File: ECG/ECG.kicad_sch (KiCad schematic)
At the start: 86 parts, among them J1 Conn_01x03, J10 Socket 1x15, J11 Shunt block, J12 Shunt block, J13 Shunt block, J14 Shunt block, J15 Shunt block, J2 Conn_01x03, J3 Conn_01x15, J4 Conn_01x15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

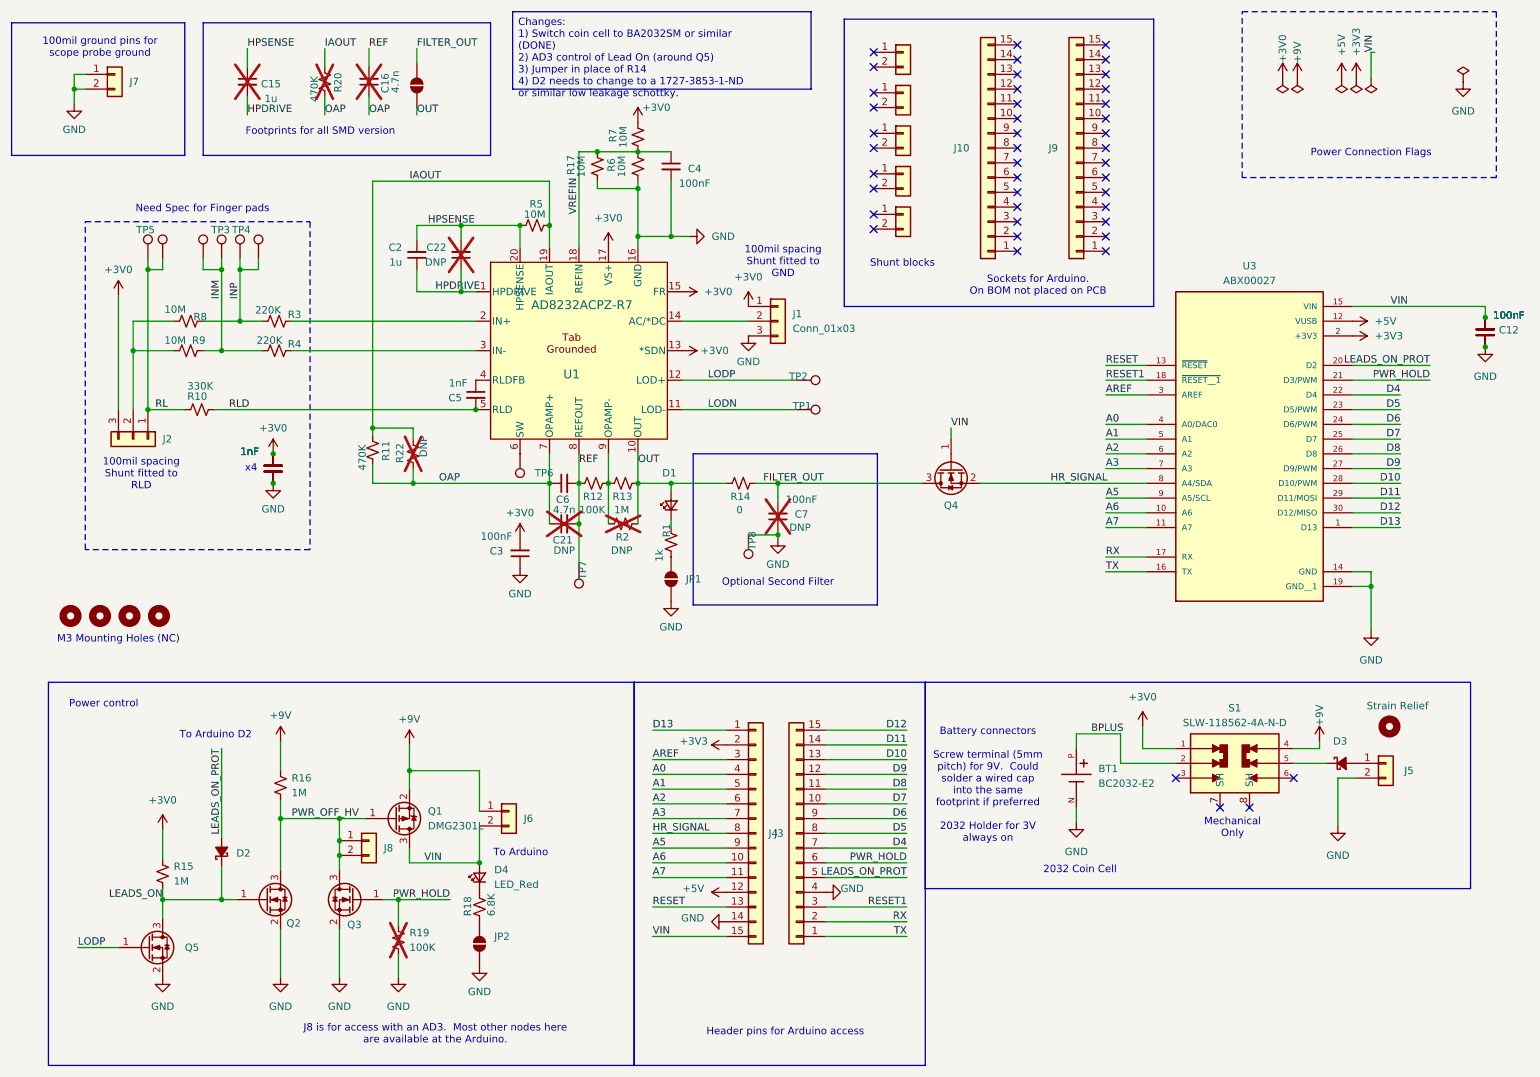
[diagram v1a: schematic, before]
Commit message: Add control of LeadsOn from AD3
Close #16
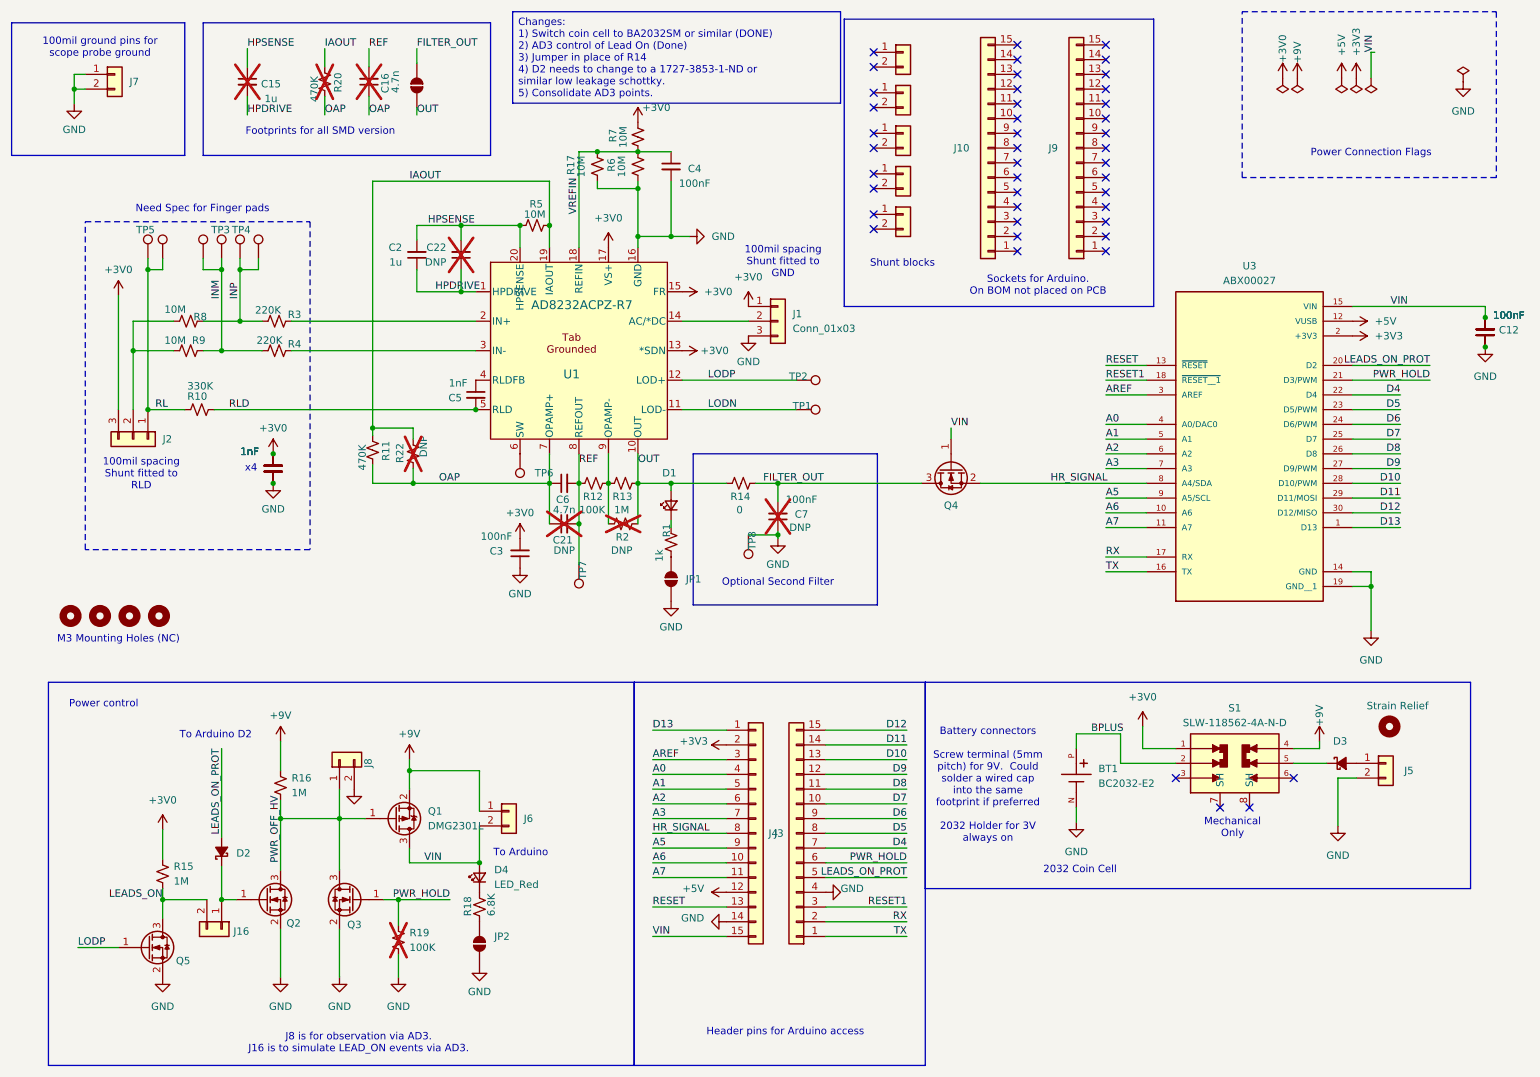
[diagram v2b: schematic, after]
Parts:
- added J16: Conn_01x02, Connector_PinHeader_2.54mm:PinHeader_1x02_P2.54mm_Vertical, symbol Connector_Generic:Conn_01x02
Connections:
- net GND: now also J8.2 (Pin_2)
- net LEADS_ON: now also J16.2 (Pin_2); no longer D2.1 (K), Q2.1 (G)
- net PWR_OFF_HV: no longer J8.2 (Pin_2)
- new net: D2.1 (K), J16.1 (Pin_1), Q2.1 (G)
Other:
- note added: "J8 is for observation via AD3. J16 is to simulate LEAD_ON events via AD3."
- note removed: "J8 is for access with an AD3. Most other nodes here are available at the Arduino."
- moved on the sheet: J8
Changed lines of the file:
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@@
 		)
 	)
-	(text "J8 is for access with an AD3.  Most other nodes here \nare available at the Arduino."
+	(text "J8 is for observation via AD3.\nJ16 is to simulate LEAD_ON events via AD3."
 		(exclude_from_sim no)
-		(at 88.9 190.246 0)
+		(at 75.692 191.77 0)
 		(effects
 			(font
@@
 		)
 	)
-	(text_box "Changes:\n1) Switch coin cell to BA2032SM or similar (DONE)\n2) AD3 control of Lead On (around Q5)\n3) Jumper in place of R14\n4) D2 needs to change to a 1727-3853-1-ND or similar low leakage schottky."
+	(text_box "Changes:\n1) Switch coin cell to BA2032SM or similar (DONE)\n2) AD3 control of Lead On (Done)\n3) Jumper in place of R14\n4) D2 needs to change to a 1727-3853-1-ND or similar low leakage schottky.\n5) Consolidate AD3 points."
 		(exclude_from_sim no)
 		(at 102.235 13.97 0)
-		(size 51.435 13.335)
+		(size 56.515 15.748)
 		(margins 0.9525 0.9525 0.9525 0.9525)
 		(stroke
@@
 	)
 	(junction
-		(at 72.39 159.385)
-		(diameter 0)
-		(color 0 0 0 0)
-	)
-	(junction
 		(at 41.91 167.005)
 		(diameter 0)
@@
 	)
 	(junction
-		(at 72.39 156.845)
-		(diameter 0)
-		(color 0 0 0 0)
-	)
-	(junction
 		(at 62.23 153.035)
 		(diameter 0)
@@
 	(wire
 		(pts
-			(xy 72.39 156.845) (xy 72.39 159.385)
+			(xy 72.39 153.035) (xy 72.39 161.925)
 		)
 		(stroke
@@
 	(wire
 		(pts
-			(xy 84.455 140.335) (xy 84.455 144.78)
-		)
-		(stroke
-			(width 0)
-			(type default)
-		)
-	)
-	(wire
-		(pts
 			(xy 96.52 144.78) (xy 84.455 144.78)
 		)
@@
 	(wire
 		(pts
-			(xy 72.39 159.385) (xy 72.39 161.925)
-		)
-		(stroke
-			(width 0)
-			(type default)
-		)
-	)
-	(wire
-		(pts
 			(xy 116.84 43.18) (xy 116.84 44.45)
 		)
@@
 	(wire
 		(pts
-			(xy 72.39 153.035) (xy 72.39 156.845)
-		)
-		(stroke
-			(width 0)
-			(type default)
-		)
-	)
-	(wire
-		(pts
 			(xy 207.01 143.51) (xy 216.535 143.51)
 		)
@@
 	(wire
 		(pts
+			(xy 72.39 147.955) (xy 72.39 153.035)
+		)
+		(stroke
+			(width 0)
+			(type default)
+		)
+	)
+	(wire
+		(pts
 			(xy 62.23 149.86) (xy 62.23 153.035)
 		)
@@
 	(wire
 		(pts
+			(xy 84.455 142.875) (xy 84.455 144.78)
+		)
+		(stroke
+			(width 0)
+			(type default)
+		)
+	)
+	(wire
+		(pts
 			(xy 129.54 101.6) (xy 129.54 102.87)
 		)
@@
 	(wire
 		(pts
-			(xy 41.91 167.005) (xy 52.07 167.005)
+			(xy 41.91 167.005) (xy 49.53 167.005)
 		)
 		(stroke
@@
 	)
 	(label "PWR_OFF_HV"
-		(at 64.135 153.035 0)
+		(at 62.23 160.655 90)
 		(effects
 			(font
@@
 		(on_board yes)
 		(dnp no)
-		(fields_autoplaced yes)
 		(property "Reference" "Q5"
-			(at 45.72 175.2599 0)
+			(at 44.196 177.546 0)
 			(effects
 				(font
@@
 	)
 	(symbol
+		(lib_id "power:GND")
+		(at 74.93 147.955 0)
+		(unit 1)
+		(exclude_from_sim no)
+		(in_bom yes)
+		(on_board yes)
+		(dnp no)
+		(property "Reference" "#PWR042"
+			(at 74.93 154.305 0)
+			(effects
+				(font
+					(size 1.27 1.27)
+				)
+				(hide yes)
+			)
+		)
+		(property "Value" "GND"
+			(at 77.851 150.876 0)
+			(effects
+				(font
+					(size 1.27 1.27)
+				)
+				(hide yes)
+			)
+		)
+		(property "Footprint" ""
+			(at 74.93 147.955 0)
+			(effects
+				(font
+					(size 1.27 1.27)
+				)
+				(hide yes)
+			)
+		)
+		(property "Datasheet" ""
+			(at 74.93 147.955 0)
+			(effects
+				(font
+					(size 1.27 1.27)
+				)
+				(hide yes)
+			)
+		)
+		(property "Description" "Power symbol creates a global label with name \"GND\" , ground"
+			(at 74.93 147.955 0)
+			(effects
+				(font
+					(size 1.27 1.27)
+				)
+				(hide yes)
+			)
+		)
+		(pin "1"
+		)
+		(instances
+			(project "ECG"
+				(path "/e3a79443-8349-4546-8b4f-331bcc551083"
+					(reference "#PWR042")
+					(unit 1)
+				)
+			)
+		)
+	)
+	(symbol
 		(lib_id "Mechanical:MountingHole")
 		(at 31.115 118.11 0)
@@
 	(symbol
 		(lib_id "power:+9V")
-		(at 84.455 140.335 0)
+		(at 84.455 142.875 0)
 		(mirror y)
 		(unit 1)
@@
 		(fields_autoplaced yes)
 		(property "Reference" "#PWR02"
-			(at 84.455 144.145 0)
+			(at 84.455 146.685 0)
 			(effects
 				(font
@@
 		)
 		(property "Value" "+9V"
-			(at 84.455 135.89 0)
+			(at 84.455 138.43 0)
 			(effects
 				(font
@@
 		)
 		(property "Footprint" ""
-			(at 84.455 140.335 0)
+			(at 84.455 142.875 0)
 			(effects
 				(font
@@
 		)
 		(property "Datasheet" ""
-			(at 84.455 140.335 0)
+			(at 84.455 142.875 0)
 			(effects
 				(font
@@
 		)
 		(property "Description" "Power symbol creates a global label with name \"+9V\""
-			(at 84.455 140.335 0)
+			(at 84.455 142.875 0)
 			(effects
 				(font
@@
 	(symbol
 		(lib_id "Connector_Generic:Conn_01x02")
-		(at 77.47 156.845 0)
+		(at 72.39 142.875 90)
 		(unit 1)
 		(exclude_from_sim no)
@@
 		(on_board yes)
 		(dnp no)
-		(fields_autoplaced yes)
 		(property "Reference" "J8"
-			(at 80.01 158.1149 0)
+			(at 77.343 144.272 0)
 			(effects
 				(font
@@
 		)
 		(property "Value" "Conn_01x02"
-			(at 80.01 159.3849 0)
+			(at 74.9299 140.335 0)
 			(effects
 				(font
@@
 		)
 		(property "Footprint" "Connector_PinHeader_2.54mm:PinHeader_1x02_P2.54mm_Vertical"
-			(at 77.47 156.845 0)
+			(at 72.39 142.875 0)
 			(effects
 				(font
@@
 		)
 		(property "Datasheet" "~"
-			(at 77.47 156.845 0)
+			(at 72.39 142.875 0)
 			(effects
 				(font
@@
 		)
 		(property "Description" "Generic connector, single row, 01x02, script generated (kicad-library-utils/schlib/autogen/connector/)"
-			(at 77.47 156.845 0)
+			(at 72.39 142.875 0)
 			(effects
 				(font
@@
 		)
 		(property "Sim.Device" ""
-			(at 77.47 156.845 0)
+			(at 72.39 142.875 0)
 			(effects
 				(font
@@
 		)
 		(property "Sim.Pins" ""
-			(at 77.47 156.845 0)
+			(at 72.39 142.875 0)
 			(effects
 				(font
@@
 		)
 		(property "DigikeyPN" "2057-PH1-02-UA-ND"
-			(at 77.47 156.845 0)
+			(at 72.39 142.875 0)
 			(effects
 				(font
@@
 					(unit 1)
 				)
+			)
+		)
+	)
+	(symbol
+		(lib_id "Connector_Generic:Conn_01x02")
+		(at 52.07 172.085 270)
+		(unit 1)
+		(exclude_from_sim no)
+		(in_bom yes)
+		(on_board yes)
+		(dnp no)
+		(property "Reference" "J16"
+			(at 54.102 172.466 90)
+			(effects
+				(font
+					(size 1.27 1.27)
+				)
+				(justify left)
+			)
+		)
+		(property "Value" "Conn_01x02"
+			(at 49.5301 174.625 0)
+			(effects
+				(font
+					(size 1.27 1.27)
+				)
+				(justify left)
+				(hide yes)
+			)
+		)
+		(property "Footprint" "Connector_PinHeader_2.54mm:PinHeader_1x02_P2.54mm_Vertical"
+			(at 52.07 172.085 0)
+			(effects
+				(font
+					(size 1.27 1.27)
+				)
+				(hide yes)
+			)
+		)
+		(property "Datasheet" "~"
+			(at 52.07 172.085 0)
+			(effects
+				(font
+					(size 1.27 1.27)
+				)
+				(hide yes)
+			)
+		)
+		(property "Description" "Generic connector, single row, 01x02, script generated (kicad-library-utils/schlib/autogen/connector/)"
+			(at 52.07 172.085 0)
+			(effects
+				(font
+					(size 1.27 1.27)
+				)
+				(hide yes)
+			)
+		)
+		(property "Sim.Device" ""
+			(at 52.07 172.085 0)
+			(effects
+				(font
+					(size 1.27 1.27)
+				)
+				(hide yes)
+			)
+		)
+		(property "Sim.Pins" ""
+			(at 52.07 172.085 0)
+			(effects
+				(font
+					(size 1.27 1.27)
+				)
+				(hide yes)
+			)
+		)
+		(property "DigikeyPN" "2057-PH1-02-UA-ND"
+			(at 52.07 172.085 0)
+			(effects
+				(font
+					(size 1.27 1.27)
+				)
+				(hide yes)
+			)
+		)
+		(pin "1"
+		)
+		(pin "2"
+		)
+		(instances
+			(project "ECG"
+				(path "/e3a79443-8349-4546-8b4f-331bcc551083"
+					(reference "J16")
+					(unit 1)
+				)

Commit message: Work on AD3 connection stuff
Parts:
- removed J16, J8: Conn_01x02, Connector_PinHeader_2.54mm:PinHeader_1x02_P2.54mm_Vertical, symbol Connector_Generic:Conn_01x02
- removed JP3: SolderJumper_2_Open, Jumper:SolderJumper-2_P1.3mm_Open_RoundedPad1.0x1.5mm, symbol Jumper:SolderJumper_2_Open
- added J8: Conn_02x05_Odd_Even, Connector_PinSocket_2.54mm:PinSocket_2x05_P2.54mm_Vertical, symbol Connector_Generic:Conn_02x05_Odd_Even
- added JP3: SolderJumper_2_Bridged, Jumper:SolderJumper-2_P1.3mm_Bridged_RoundedPad1.0x1.5mm, symbol StockedComponents:SolderJumper_2_Bridged
- D2: DigikeyPN CRS01QCT-ND -> 1727-3853-1-ND
- J10, J11, J12, J13, J14, J15, J9, R14: now not fitted
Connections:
- net FILTER_OUT: now also JP3.2 (B)
- net GND: now also J8.5 (Pin_5), J8.7 (Pin_7), J8.9 (Pin_9)
- net LEADS_ON: now also J8.1 (Pin_1)
- net OUT: now also J8.10 (Pin_10), JP3.1 (A)
- net PWR_OFF_HV: now also J8.8 (Pin_8)
- net at D2.1 (K), Q2.1 (G): now also J8.2 (Pin_2), J8.3 (Pin_3)
- new net: J8.4 (Pin_4), J8.6 (Pin_6)
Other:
- note added: "J16 - Normal operation has a jumper fitted across pins 1-2. Current value can be observed between 3-5. To simulate LEAD-ON/OFF events, the students must move the shunt to pins 3-4 and connect the AD3 across 5-6. 9V version can be observed at 7-8."
- note added: "J6 can be fitted to bypass power control"
- note added: "Sockets for Arduino. On BOM not placed on board. U2 has the THT for these. They will be populated."
- note removed: "J8 is for observation via AD3. J16 is to simulate LEAD_ON events via AD3."
- note removed: "Sockets for Arduino. On BOM not placed on PCB"
- moved on the sheet: D2, D4, J6, JP2, Q1, Q2, Q3, Q5, R15, R16, R18, R19

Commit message: Manually merge commit d0bb662.
Low leakage schottky for protection.
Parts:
- D2: footprint Diode_SMD:D_SOD-123F -> Diode_SMD:D_SOD-123; DigikeyPN 1727-3853-1-ND -> SM5817PL-TPMSCT-ND
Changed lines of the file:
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@@
 			)
 		)
-		(property "Footprint" "Diode_SMD:D_SOD-123F"
+		(property "Footprint" "Diode_SMD:D_SOD-123"
 			(at 63.5 155.575 90)
 			(effects
@@
 			)
 		)
-		(property "DigikeyPN" "1727-3853-1-ND"
+		(property "DigikeyPN" "SM5817PL-TPMSCT-ND"
 			(at 63.5 155.575 0)
 			(effects

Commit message: cleanup layout
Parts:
- D3: footprint Diode_SMD:D_SOD-123F -> Diode_SMD:D_SOD-123; DigikeyPN CRS01QCT-ND -> SM5817PL-TPMSCT-ND
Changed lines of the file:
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@@
 	)
 	(symbol
+		(lib_id "Device:D_Schottky_Small_Filled")
+		(at 245.11 143.51 0)
+		(unit 1)
+		(exclude_from_sim no)
+		(in_bom yes)
+		(on_board yes)
+		(dnp no)
+		(fields_autoplaced yes)
+		(property "Reference" "D3"
+			(at 244.856 140.335 0)
+			(effects
+				(font
+					(size 1.27 1.27)
+				)
+			)
+		)
+		(property "Value" "~"
+			(at 244.856 140.335 0)
+			(effects
+				(font
+					(size 1.27 1.27)
+				)
+				(hide yes)
+			)
+		)
+		(property "Footprint" "Diode_SMD:D_SOD-123"
+			(at 245.11 143.51 90)
+			(effects
+				(font
+					(size 1.27 1.27)
+				)
+				(hide yes)
+			)
+		)
+		(property "Datasheet" "~"
+			(at 245.11 143.51 90)
+			(effects
+				(font
+					(size 1.27 1.27)
+				)
+				(hide yes)
+			)
+		)
+		(property "Description" "Schottky diode, low leakage"
+			(at 245.11 143.51 0)
+			(effects
+				(font
+					(size 1.27 1.27)
+				)
+				(hide yes)
+			)
+		)
+		(property "DigikeyPN" "SM5817PL-TPMSCT-ND"
+			(at 245.11 143.51 0)
+			(effects
+				(font
+					(size 1.27 1.27)
+				)
+				(hide yes)
+			)
+		)
+		(property "Sim.Device" ""
+			(at 245.11 143.51 90)
+			(effects
+				(font
+					(size 1.27 1.27)
+				)
+				(hide yes)
+			)
+		)
+		(property "Sim.Pins" ""
+			(at 245.11 143.51 90)
+			(effects
+				(font
+					(size 1.27 1.27)
+				)
+				(hide yes)
+			)
+		)
+		(pin "1"
+		)
+		(pin "2"
+		)
+		(instances
+			(project "ECG"
+				(path "/e3a79443-8349-4546-8b4f-331bcc551083"
+					(reference "D3")
+					(unit 1)
+				)
+			)
+		)
+	)
+	(symbol
 		(lib_id "power:+5V")
 		(at 245.11 25.4 0)
@@
 					(unit 1)
 				)
-			)
-		)
-	)
-	(symbol
-		(lib_id "Device:D_Schottky_Small_Filled")
-		(at 245.11 143.51 0)
-		(unit 1)
-		(exclude_from_sim no)
-		(in_bom yes)
-		(on_board yes)
-		(dnp no)
-		(fields_autoplaced yes)
-		(property "Reference" "D3"
-			(at 244.856 139.7 0)
-			(effects
-				(font
-					(size 1.27 1.27)
-				)
-			)
-		)
-		(property "Value" "~"
-			(at 244.856 140.335 0)
-			(effects
-				(font
-					(size 1.27 1.27)
-				)
-				(hide yes)
-			)
-		)
-		(property "Footprint" "Diode_SMD:D_SOD-123F"
-			(at 245.11 143.51 90)
-			(effects
-				(font
-					(size 1.27 1.27)
-				)
-				(hide yes)
-			)
-		)
-		(property "Datasheet" "~"
-			(at 245.11 143.51 90)
-			(effects
-				(font
-					(size 1.27 1.27)
-				)
-				(hide yes)
-			)
-		)
-		(property "Description" "Schottky diode, small symbol, filled shape"
-			(at 245.11 143.51 0)
-			(effects
-				(font
-					(size 1.27 1.27)
-				)
-				(hide yes)
-			)
-		)
-		(property "DigikeyPN" "CRS01QCT-ND"
-			(at 245.11 143.51 0)
-			(effects
-				(font
-					(size 1.27 1.27)
-				)
-				(hide yes)
-			)
-		)
-		(property "Sim.Device" ""
-			(at 245.11 143.51 0)
-			(effects
-				(font
-					(size 1.27 1.27)
-				)
-				(hide yes)
-			)
-		)
-		(property "Sim.Pins" ""
-			(at 245.11 143.51 0)
-			(effects
-				(font
-					(size 1.27 1.27)
-				)
-				(hide yes)
-			)
-		)
-		(pin "1"
-		)
-		(pin "2"
-		)
-		(instances
-			(project ""
-				(path "/e3a79443-8349-4546-8b4f-331bcc551083"
-					(reference "D3")
-					(unit 1)
-				)

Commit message: Cleanup layout.
Close #17
Close #15
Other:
- note added: "J8 - Normal operation has a jumper fitted across pins 1-2. Logic level can be observed between 3-5. To simulate LEAD-ON/OFF events, the students must move the shunt to pins 3-4 and connect the AD3 across 5-6. Inverted 9V version can be observed at 7-8. Amplifier output can be see between pins 9 and 10."
- note removed: "J16 - Normal operation has a jumper fitted across pins 1-2. Current value can be observed between 3-5. To simulate LEAD-ON/OFF events, the students must move the shunt to pins 3-4 and connect the AD3 across 5-6. 9V version can be observed at 7-8."
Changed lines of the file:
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@@
 		)
 	)
-	(text "J16 - Normal operation has a jumper fitted across pins 1-2.  Current value can \nbe observed between 3-5.  To simulate LEAD-ON/OFF events, the students must move \nthe shunt to pins 3-4 and connect the AD3 across 5-6.  9V version can be observed \nat 7-8.\n"
+	(text "J8 - Normal operation has a jumper fitted across pins 1-2.  Logic level can \nbe observed between 3-5.  To simulate LEAD-ON/OFF events, the students must move \nthe shunt to pins 3-4 and connect the AD3 across 5-6.  Inverted 9V version can \nbe observed at 7-8.  Amplifier output can be see between pins 9 and 10.\n"
 		(exclude_from_sim no)
 		(at 22.606 189.992 0)
@@
 		)
 	)
-	(text_box "Changes:\n1) Switch coin cell to BA2032SM or similar (DONE)\n2) AD3 control of Lead On (Done)\n3) Jumper in place of R14 (Done)\n4) D2 needs to change to a 1727-3853-1-ND or similar low leakage schottky. (Done)\n5) Consolidate AD3 points."
+	(text_box "Changes:\n1) Switch coin cell to BA2032SM or similar (DONE)\n2) AD3 control of Lead On (Done)\n3) Jumper in place of R14 (Done)\n4) D2 needs to change to a 1727-3853-1-ND or similar low leakage schottky. (Done)\n5) Consolidate AD3 points. (Done)"
 		(exclude_from_sim no)
 		(at 102.235 13.97 0)
@@
 		(on_board yes)
 		(dnp no)
-		(fields_autoplaced yes)
 		(property "Reference" "J8"
-			(at 54.61 160.02 0)
+			(at 54.356 161.29 0)
 			(effects
 				(font
@@
 		(dnp no)
 		(property "Reference" "C6"
-			(at 110.871 98.044 90)
+			(at 158.75 81.534 90)
 			(effects
 				(font

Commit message: work on manufacturing
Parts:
- TP1, TP2, TP3, TP4, TP5, TP6, TP7, TP8: now not fitted
